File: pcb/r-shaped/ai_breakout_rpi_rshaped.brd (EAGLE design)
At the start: 58.4 x 17.8 mm, 4 parts

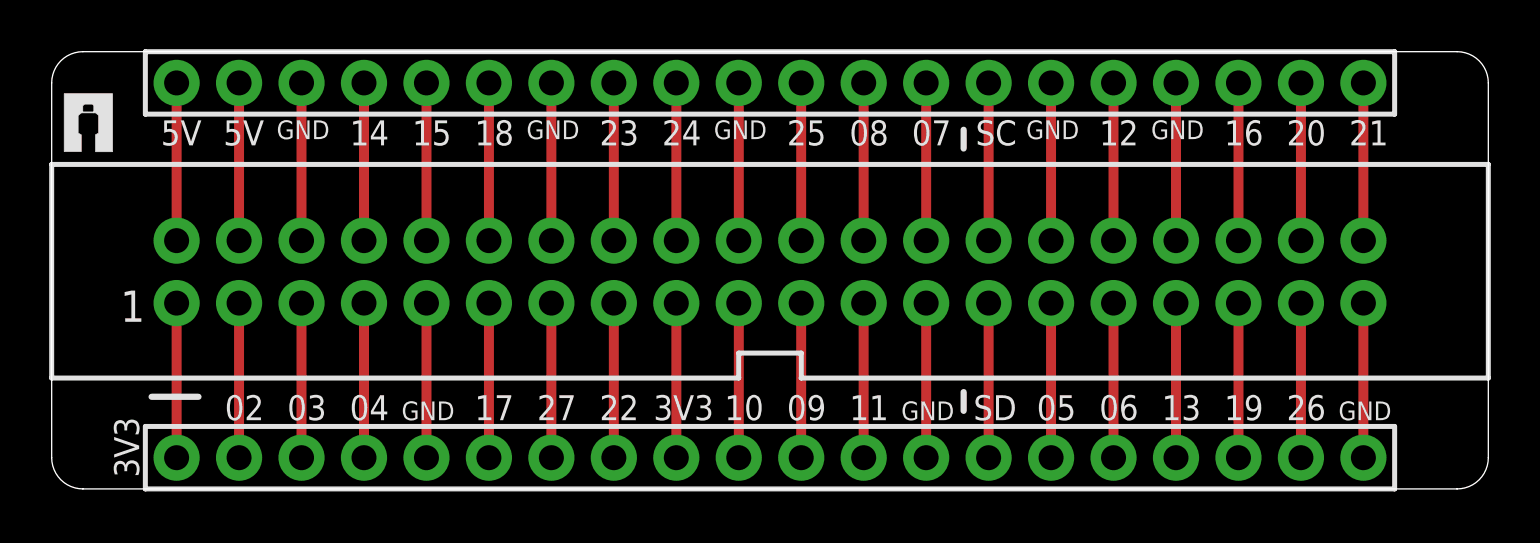
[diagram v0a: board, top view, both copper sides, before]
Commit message: Updating T-Shaped.  Added a few labels to R-Shaped
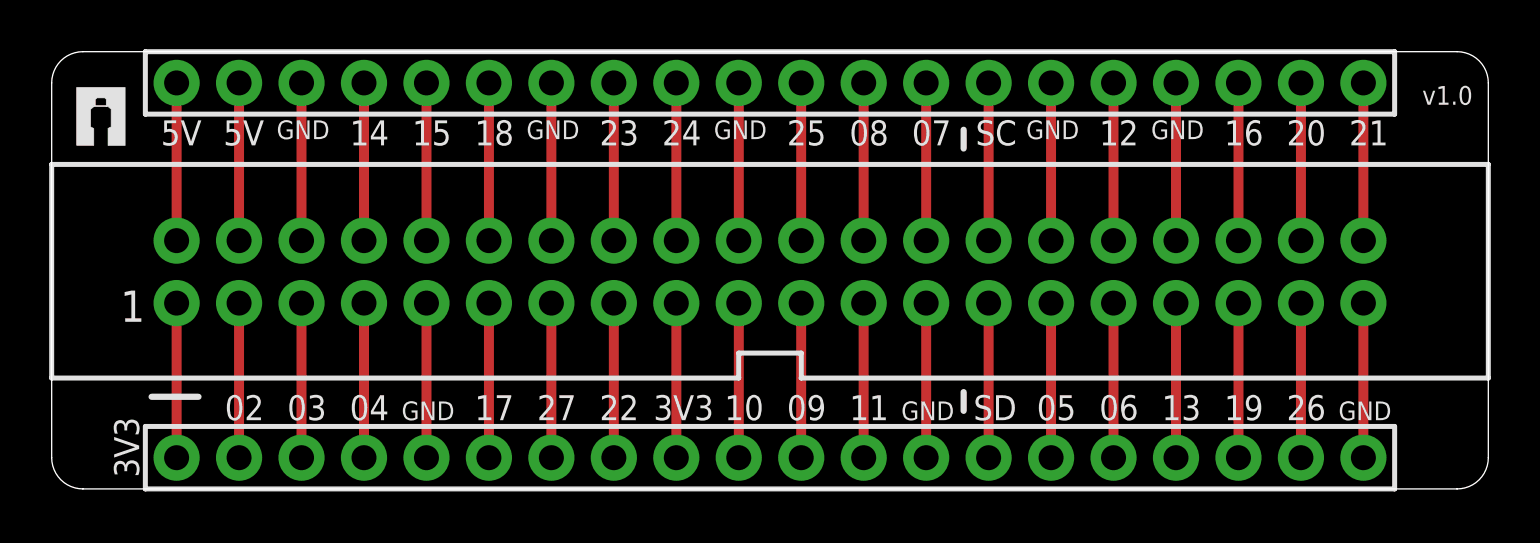
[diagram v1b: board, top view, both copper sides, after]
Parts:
- added U$2: AI-LOGOXS, Ai_Miscellany:AI-LOGO-XS
- moved U$1 0.57 mm to (1.02, 14.0)
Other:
- board text added: "v1.0"
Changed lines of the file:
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@@
 <?xml version="1.0" encoding="utf-8"?>
 <!DOCTYPE eagle SYSTEM "eagle.dtd">
-<eagle version="7.2.0">
+<eagle version="7.1.0">
 <drawing>
 <settings>
@@
 <setting verticaltext="up"/>
 </settings>
-<grid distance="10" unitdist="mil" unit="mil" style="lines" multiple="1" display="yes" altdistance="0.025" altunitdist="inch" altunit="inch"/>
+<grid distance="5" unitdist="mil" unit="mil" style="lines" multiple="1" display="yes" altdistance="0.025" altunitdist="inch" altunit="inch"/>
 <layers>
-<layer number="1" name="Top" color="4" fill="1" visible="no" active="yes"/>
+<layer number="1" name="Top" color="4" fill="1" visible="yes" active="yes"/>
 <layer number="2" name="Route2" color="1" fill="3" visible="no" active="no"/>
 <layer number="15" name="Route15" color="4" fill="6" visible="no" active="no"/>
-<layer number="16" name="Bottom" color="1" fill="1" visible="no" active="yes"/>
+<layer number="16" name="Bottom" color="1" fill="1" visible="yes" active="yes"/>
 <layer number="17" name="Pads" color="2" fill="1" visible="yes" active="yes"/>
 <layer number="18" name="Vias" color="2" fill="1" visible="yes" active="yes"/>
@@
 <layer number="20" name="Dimension" color="15" fill="1" visible="yes" active="yes"/>
 <layer number="21" name="tPlace" color="7" fill="1" visible="yes" active="yes"/>
-<layer number="22" name="bPlace" color="7" fill="1" visible="no" active="yes"/>
+<layer number="22" name="bPlace" color="7" fill="1" visible="yes" active="yes"/>
 <layer number="23" name="tOrigins" color="15" fill="1" visible="yes" active="yes"/>
 <layer number="24" name="bOrigins" color="15" fill="1" visible="yes" active="yes"/>
 <layer number="25" name="tNames" color="7" fill="1" visible="yes" active="yes"/>
 <layer number="26" name="bNames" color="7" fill="1" visible="yes" active="yes"/>
-<layer number="27" name="tValues" color="7" fill="1" visible="no" active="yes"/>
-<layer number="28" name="bValues" color="7" fill="1" visible="no" active="yes"/>
+<layer number="27" name="tValues" color="7" fill="1" visible="yes" active="yes"/>
+<layer number="28" name="bValues" color="7" fill="1" visible="yes" active="yes"/>
 <layer number="29" name="tStop" color="7" fill="3" visible="no" active="yes"/>
 <layer number="30" name="bStop" color="7" fill="6" visible="no" active="yes"/>
@@
 <layer number="42" name="bRestrict" color="1" fill="10" visible="no" active="yes"/>
 <layer number="43" name="vRestrict" color="2" fill="10" visible="no" active="yes"/>
-<layer number="44" name="Drills" color="7" fill="1" visible="yes" active="yes"/>
-<layer number="45" name="Holes" color="7" fill="1" visible="yes" active="yes"/>
+<layer number="44" name="Drills" color="7" fill="1" visible="no" active="yes"/>
+<layer number="45" name="Holes" color="7" fill="1" visible="no" active="yes"/>
 <layer number="46" name="Milling" color="3" fill="1" visible="no" active="yes"/>
 <layer number="47" name="Measures" color="7" fill="1" visible="no" active="yes"/>
@@
 <wire x1="0" y1="16.51" x2="1.27" y2="17.78" width="0.0254" layer="20" curve="-90"/>
 <text x="29.21" y="3.556" size="1.143" layer="22" font="vector" ratio="10" rot="MR180" align="center">https://acrobotic.com</text>
+<text x="57.785" y="16.383" size="0.762" layer="21" font="vector" ratio="10" rot="R180">v1.0</text>
 </plain>
 <attributes>
@@
 <element name="RPI_RECT" library="Ai_Connectors" package="2X20-RPI-BRK" value="2X20-RPI-BRK" x="29.21" y="8.8265" smashed="yes"/>
 <element name="LEFT" library="Ai_Connectors" package="1X20" value="1X20" x="29.21" y="1.27" smashed="yes"/>
-<element name="U$1" library="Ai_Miscellany" package="AI-LOGO-XS" value="AI-LOGOXS" x="0.508" y="13.716"/>
+<element name="U$1" library="Ai_Miscellany" package="AI-LOGO-XS" value="AI-LOGOXS" x="1.016" y="13.97"/>
+<element name="U$2" library="Ai_Miscellany" package="AI-LOGO-XS" value="AI-LOGOXS" x="57.404" y="0.381" rot="MR0"/>
 </elements>
 <signals>
